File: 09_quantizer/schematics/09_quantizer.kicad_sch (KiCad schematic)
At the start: 41 parts, among them J5 In 1, J6 In 2, U1 74HC595, U2 D168K, U3 74HC595, U4 D168K

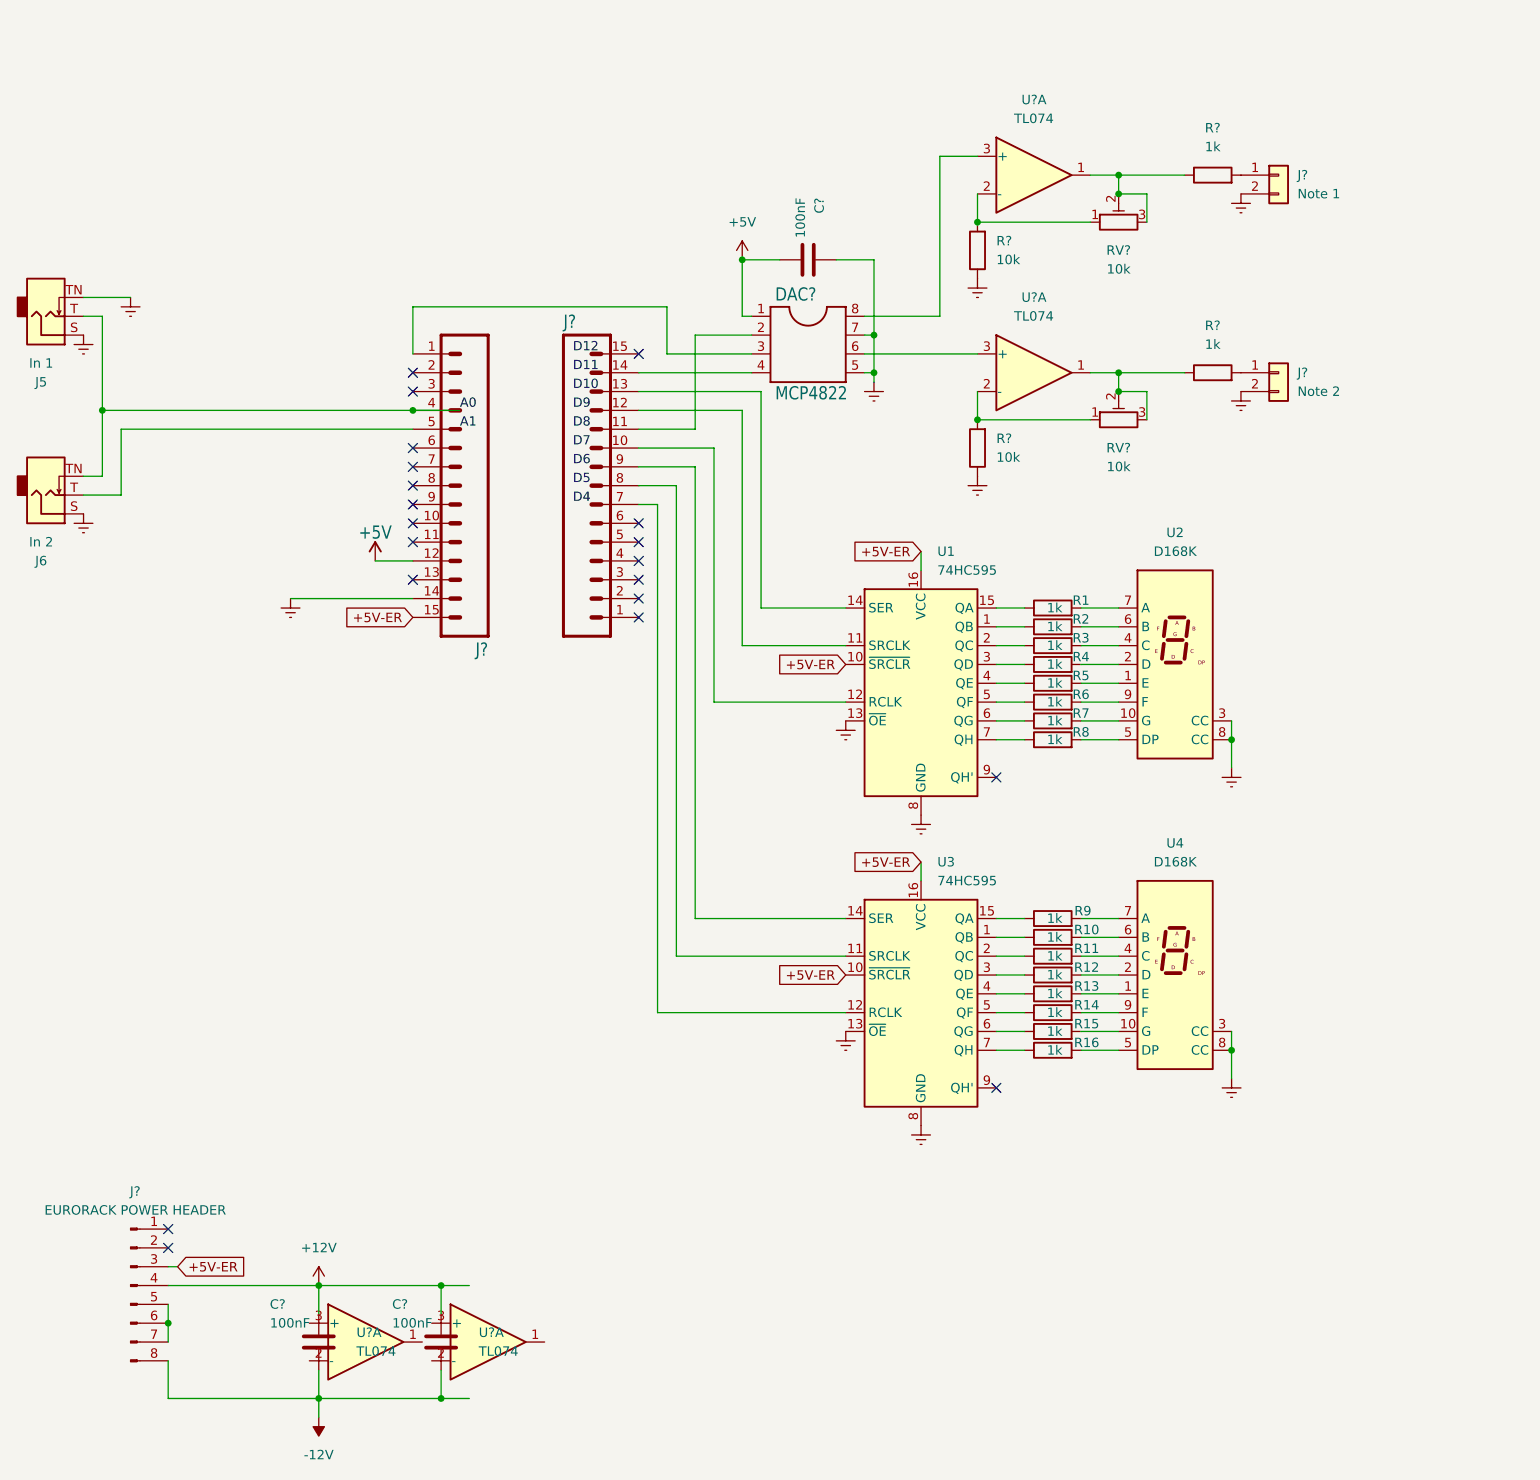
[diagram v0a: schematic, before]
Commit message: added schematics, stripboard, panel of 09
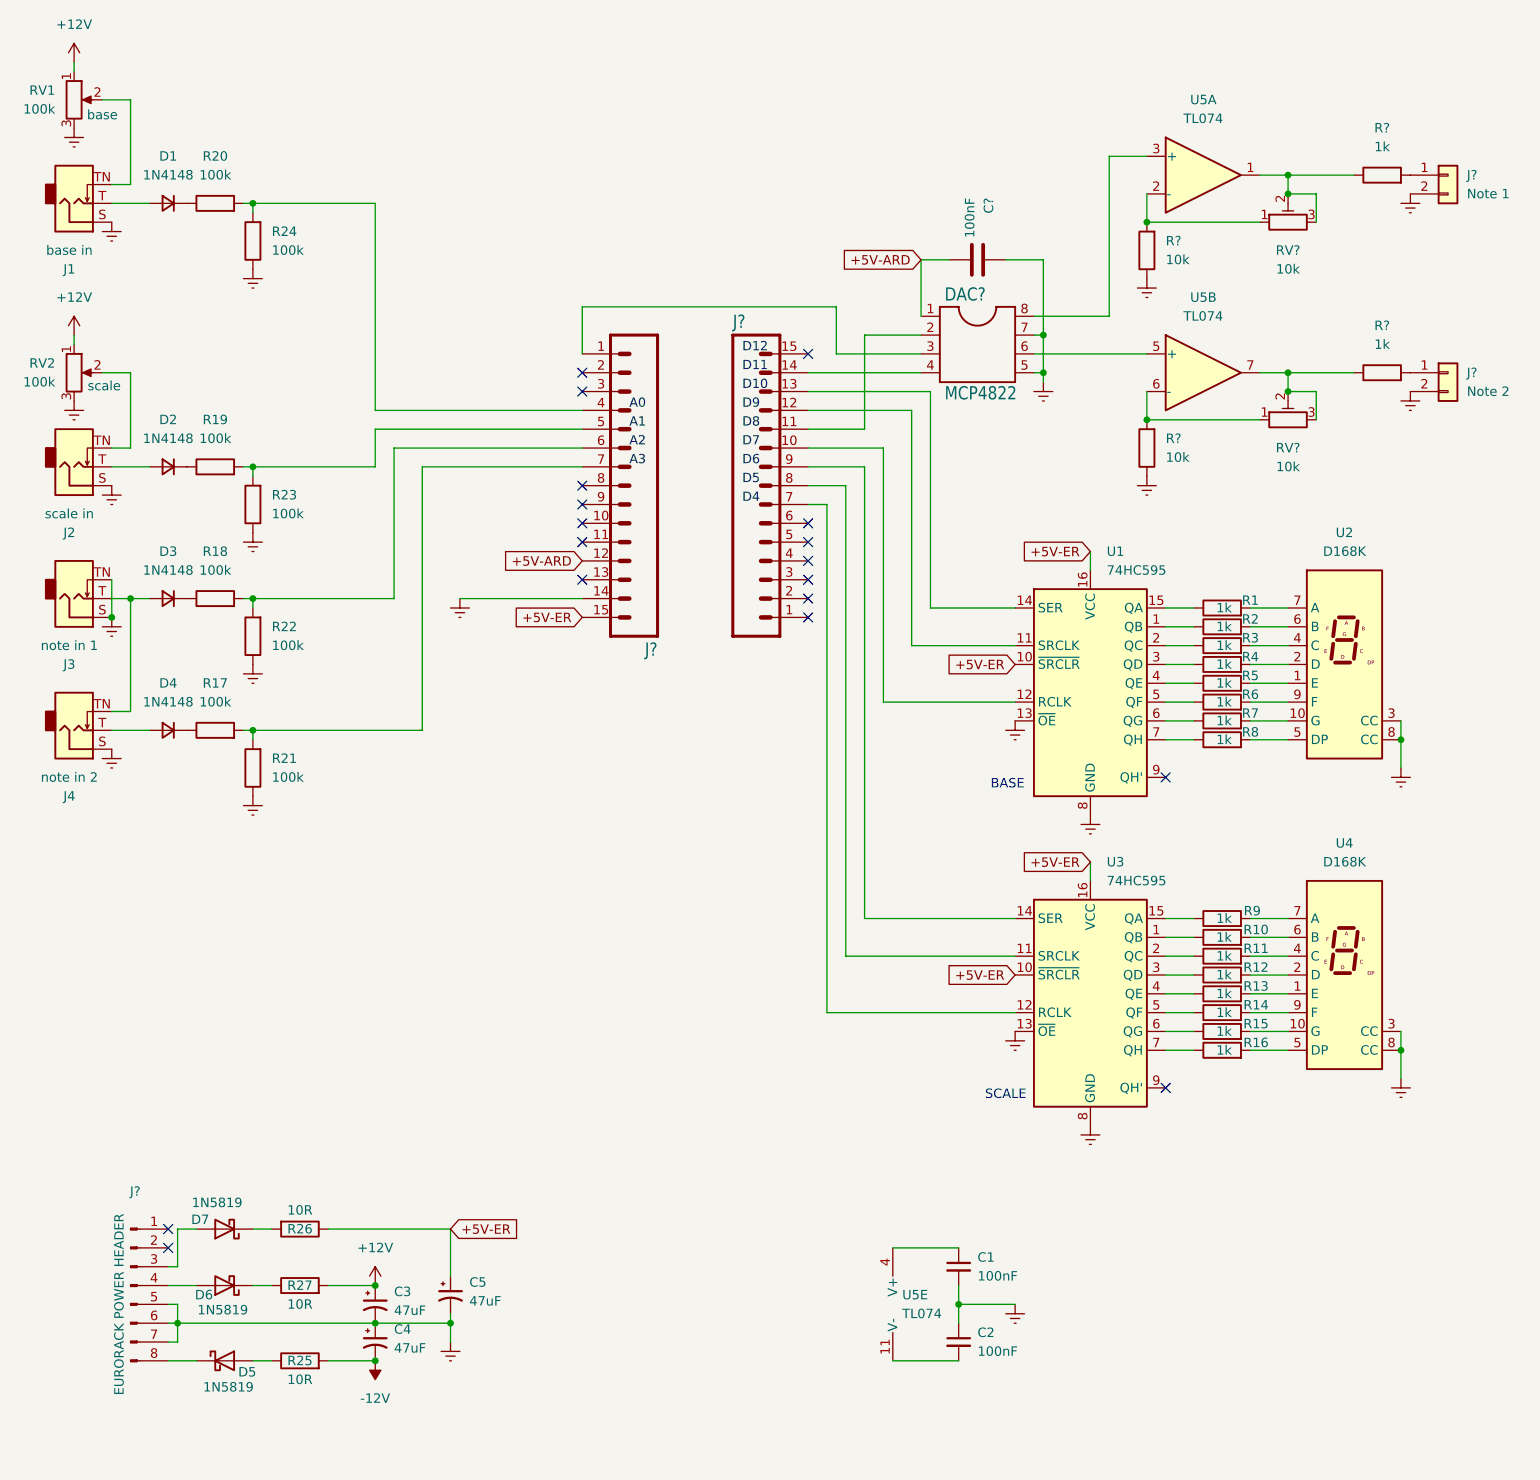
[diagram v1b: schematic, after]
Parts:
- removed C? (x2): 100nF, symbol Device:C
- removed J5: In 1, symbol Connector_Audio:AudioJack2_SwitchT
- removed J6: In 2, symbol Connector_Audio:AudioJack2_SwitchT
- removed U? (x4): TL074, symbol Amplifier_Operational:TL074
- added C1, C2: 100nF, symbol Device:C_Small
- added C3, C4, C5: 47uF, symbol Device:C_Polarized_Small_US
- added D1, D2, D3, D4: 1N4148, symbol Device:D_Small
- added D5, D6, D7: 1N5819, Diode_THT:D_DO-41_SOD81_P10.16mm_Horizontal, symbol Diode:1N5819
- added J1: base in, symbol Connector_Audio:AudioJack2_SwitchT
- added J2: scale in, symbol Connector_Audio:AudioJack2_SwitchT
- added J3: note in 1, symbol Connector_Audio:AudioJack2_SwitchT
- added J4: note in 2, symbol Connector_Audio:AudioJack2_SwitchT
- added R17, R18, R19, R20, R21, R22, R23, R24: 100k, symbol Device:R
- added R25, R26, R27: 10R, symbol Device:R
- added RV1, RV2: 100k, symbol Device:R_Potentiometer
- added U5: TL074, symbol Amplifier_Operational:TL074
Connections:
- net +12V: now also C3.1, R27.2, RV1.1, RV2.1; no longer J?.4 (Pin_4)
- net +5V-ER: now also C5.1, R26.1; no longer J?.3 (Pin_3)
- net -12V: now also C4.2, R25.2; no longer J?.8 (Pin_8)
- net A0: no longer J?.4
- net GNDREF: now also J?.5 (Pin_5), J?.6 (Pin_6), J?.7 (Pin_7), C1.2, C2.1, C3.2, C4.1, C5.2, J1.S, J2.S, J3.S, J3.TN, J4.S, R21.1, R22.1, R23.1, R24.1, RV1.3, RV2.3
- net at R?.2, RV?.1: now also U5.6 (-)
- net at R?.1, RV?.2, RV?.3: now also U5.7
- net at R?.2, RV?.1: now also U5.2 (-)
- net at R?.1, RV?.2, RV?.3: now also U5.1
- net at DAC?.8: now also U5.3 (+)
- net at DAC?.6: now also U5.5 (+)
- net at J?.5: now also R19.2, R23.2
- net at J?.6: now also R18.2, R22.2
- net at J?.7: now also R17.2, R21.2
- net +5V renamed +5V-ARD
- new net: D4.1 (K), R17.1
- new net: D4.2 (A), J4.T
- new net: C1.1, U5.4 (V+)
- new net: D1.1 (K), R20.1
- new net: D1.2 (A), J1.T
- new net: D6.1 (K), R27.1
- new net: D6.2 (A), J?.4 (Pin_4)
- new net: D7.1 (K), R26.2
- new net: D7.2 (A), J?.3 (Pin_3)
- new net: J1.TN, RV1.2
- new net: D2.1 (K), R19.1
- new net: D3.1 (K), R18.1
- new net: D3.2 (A), J3.T, J4.TN
- new net: D2.2 (A), J2.T
- new net: J?.4, R20.2, R24.2
- new net: D5.1 (K), J?.8 (Pin_8)
- new net: D5.2 (A), R25.1
- new net: J2.TN, RV2.2
- new net: C2.2, U5.11 (V-)
- no-connect marks 20 -> 18
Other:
- note added: "BASE"
- note added: "SCALE"
- moved on the sheet: C?, DAC?, J?, R1, R10, R11, R12, R13, R14, R15, R16, R2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

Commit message: fixed schematics
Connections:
- net +5V-ARD: now also U1.10 (~{SRCLR}), U1.16 (VCC), U3.10 (~{SRCLR}), U3.16 (VCC)
- net +5V-ER: no longer U1.10 (~{SRCLR}), U1.16 (VCC), U3.10 (~{SRCLR}), U3.16 (VCC)
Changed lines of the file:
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@@
+	(global_label "+5V-ARD"
+		(shape input)
+		(at 161.29 119.38 180)
+		(fields_autoplaced yes)
+		(effects
+			(font
+				(size 1.27 1.27)
+			)
+			(justify right)
+		)
+		(property "Intersheetrefs" "${INTERSHEET_REFS}"
+			(at 149.2333 119.38 0)
+			(effects
+				(font
+					(size 1.27 1.27)
+				)
+				(justify right)
+				(hide yes)
+			)
+		)
+	)
 	(global_label "+5V-ARD"
 		(shape input)
@@
 		)
 	)
-	(global_label "+5V-ER"
-		(shape input)
-		(at 151.13 134.62 180)
-		(fields_autoplaced yes)
-		(effects
-			(font
-				(size 1.27 1.27)
-			)
-			(justify right)
-		)
-		(property "Intersheetrefs" "${INTERSHEET_REFS}"
-			(at 140.2829 134.62 0)
-			(effects
-				(font
-					(size 1.27 1.27)
-				)
-				(justify right)
-				(hide yes)
-			)
-		)
-	)
 	(global_label "+5V-ARD"
 		(shape input)
@@
 		)
 	)
-	(global_label "+5V-ER"
-		(shape input)
-		(at 161.29 119.38 180)
-		(fields_autoplaced yes)
-		(effects
-			(font
-				(size 1.27 1.27)
-			)
-			(justify right)
-		)
-		(property "Intersheetrefs" "${INTERSHEET_REFS}"
-			(at 150.4429 119.38 0)
-			(effects
-				(font
-					(size 1.27 1.27)
-				)
-				(justify right)
-				(hide yes)
-			)
-		)
-	)
-	(global_label "+5V-ER"
+	(global_label "+5V-ARD"
 		(shape input)
 		(at 161.29 77.47 180)
@@
 		)
 		(property "Intersheetrefs" "${INTERSHEET_REFS}"
-			(at 150.4429 77.47 0)
+			(at 149.2333 77.47 0)
 			(effects
 				(font
@@
 		)
 	)
-	(global_label "+5V-ER"
+	(global_label "+5V-ARD"
+		(shape input)
+		(at 151.13 134.62 180)
+		(fields_autoplaced yes)
+		(effects
+			(font
+				(size 1.27 1.27)
+			)
+			(justify right)
+		)
+		(property "Intersheetrefs" "${INTERSHEET_REFS}"
+			(at 139.0733 134.62 0)
+			(effects
+				(font
+					(size 1.27 1.27)
+				)
+				(justify right)
+				(hide yes)
+			)
+		)
+	)
+	(global_label "+5V-ARD"
 		(shape input)
 		(at 151.13 92.71 180)
@@
 		)
 		(property "Intersheetrefs" "${INTERSHEET_REFS}"
-			(at 140.2829 92.71 0)
+			(at 139.0733 92.71 0)
 			(effects
 				(font
